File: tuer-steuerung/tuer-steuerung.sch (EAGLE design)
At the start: 14 parts, among them IC1 L6203, IC2 MEGA8-P, Q1 20MHz

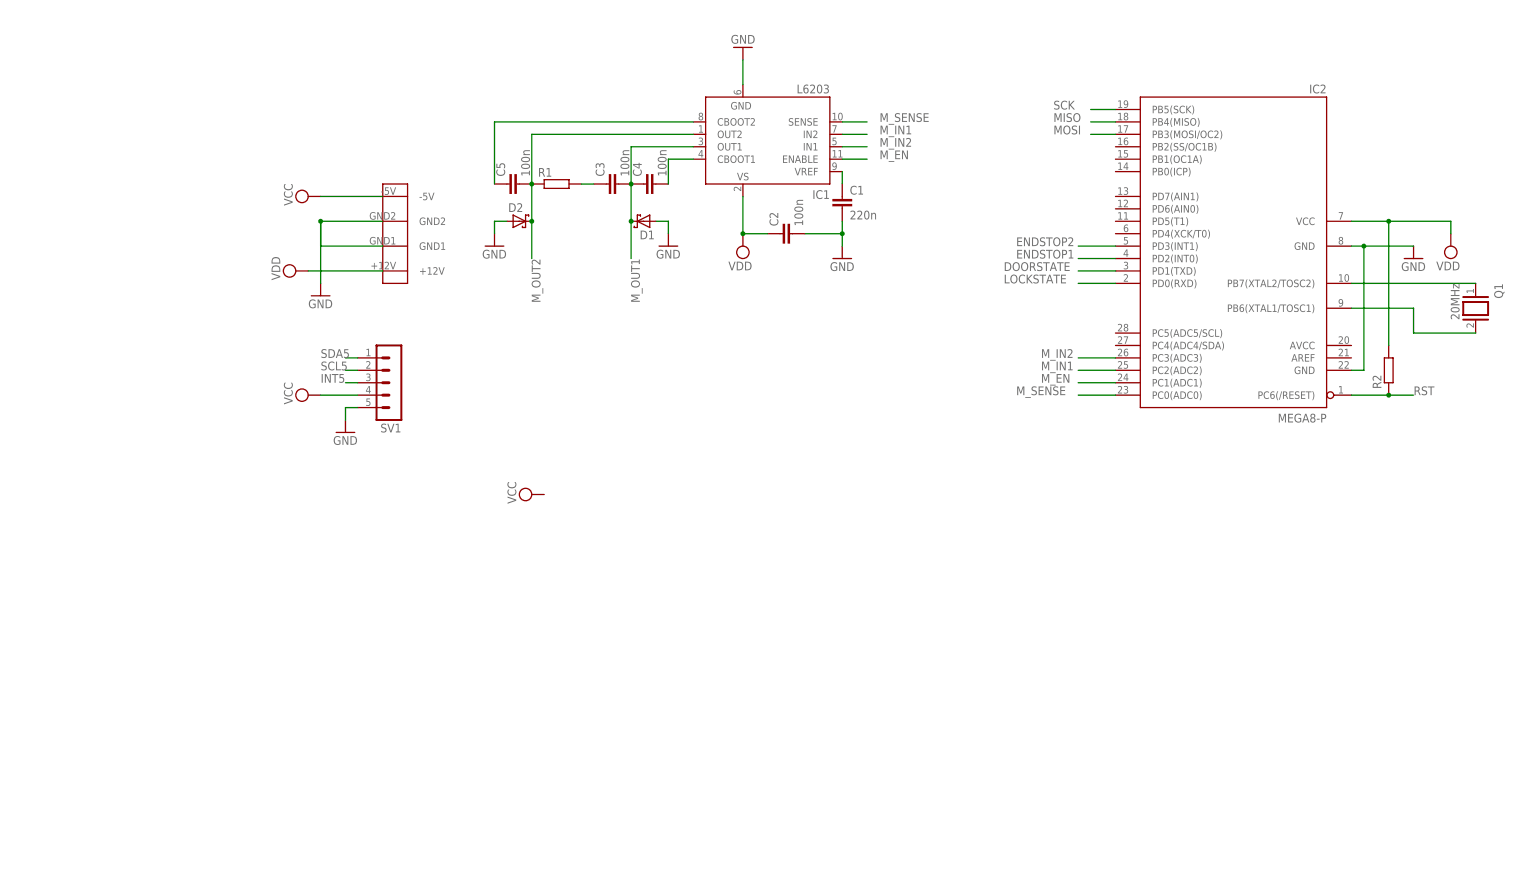
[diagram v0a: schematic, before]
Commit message: Fertige Schematics der Türsteuerung
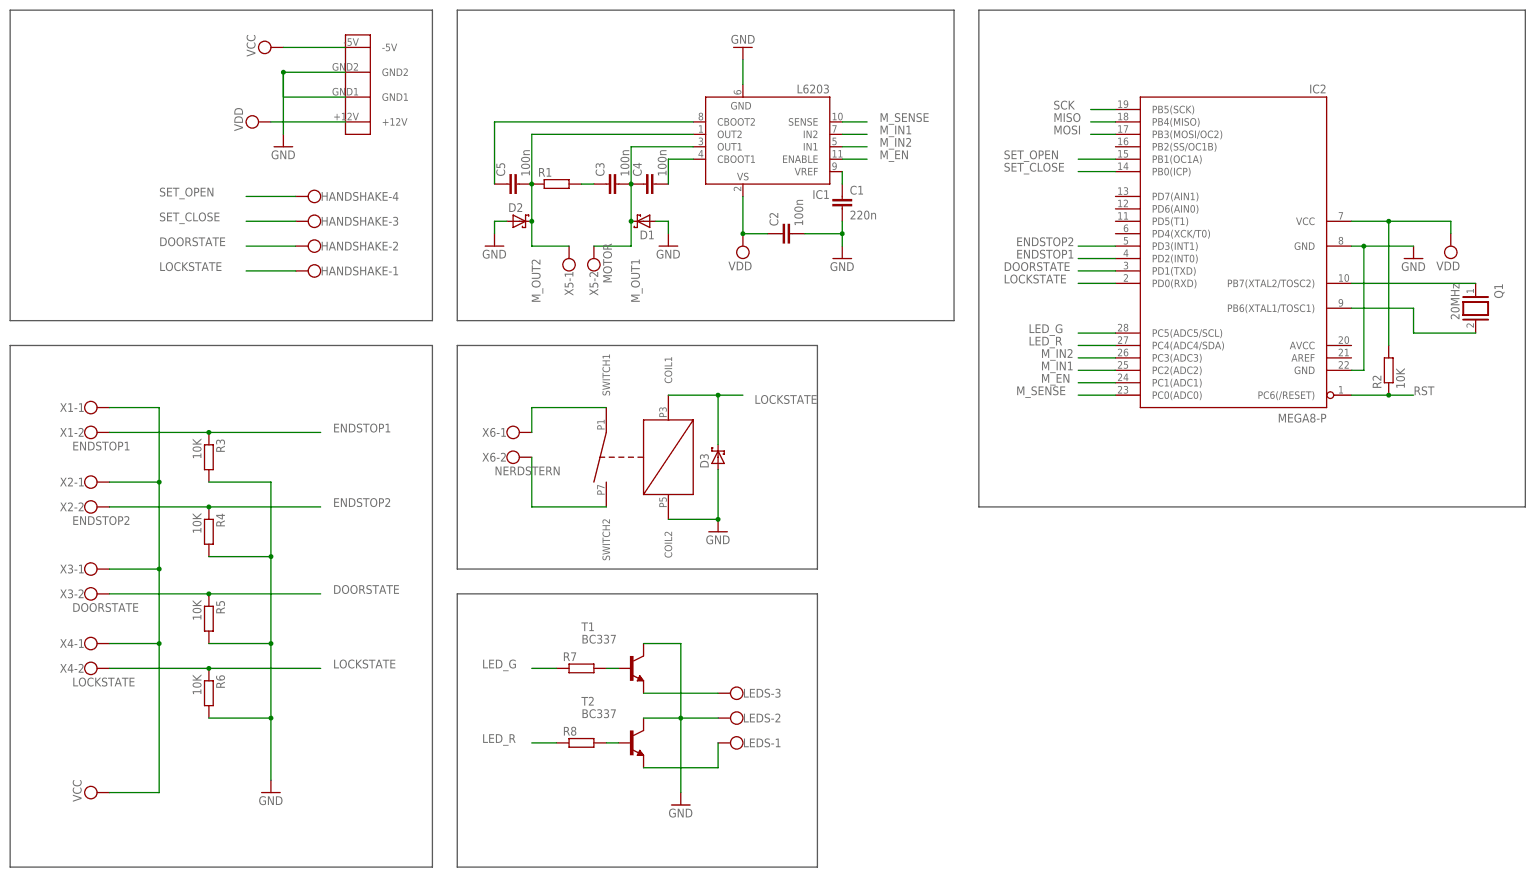
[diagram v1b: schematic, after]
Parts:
- removed SV1: (no value), con-lstb:MA05-1
- added D3: (no value), diode:SCHOTTKY-DIODEDO35-7
- added HANDSHAKE: (no value), con-wago-500:W237-4
- added LEDS: (no value), con-wago-500:W237-103
- added R3, R4, R5, R6: 10K, resistor:R-EU_0207/10
- added R7, R8: (no value), resistor:R-EU_0207/10
- added T1, T2: BC337, transistor:BC337
- added U$2: SIL05-1A72, n39:SIL05-1A72
- added X1: ENDSTOP1, con-wago-500:W237-102
- added X2: ENDSTOP2, con-wago-500:W237-102
- added X3: DOORSTATE, con-wago-500:W237-102
- added X4: LOCKSTATE, con-wago-500:W237-102
- added X5: MOTOR, con-wago-500:W237-102
- added X6: NERDSTERN, con-wago-500:W237-102
- R2: value (none) -> 10K
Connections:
- removed net INT5: SV1.3
- removed net SCL5: SV1.2
- removed net SDA5: SV1.1
- new net LED_G: IC2.PC5(ADC5/SCL), R7.1
- new net LED_R: IC2.PC4(ADC4/SDA), R8.1
- new net N$10: R8.2, T2.B
- new net N$11: LEDS-3.KL, T1.E
- new net N$12: LEDS-1.KL, T2.E
- new net N$4: X6-1.KL
- new net N$5: X6-2.KL
- new net N$9: R7.2, T1.B
- new net SET_CLOSE: HANDSHAKE-3.KL, IC2.PB0(ICP)
- new net SET_OPEN: HANDSHAKE-4.KL, IC2.PB1(OC1A)
- net DOORSTATE: now also HANDSHAKE-2.KL, R5.1, X3-2.KL
- net ENDSTOP1: now also R3.1, X1-2.KL
- net ENDSTOP2: now also R4.1, X2-2.KL
- net GND: now also D3.A, LEDS-2.KL, R3.2, R4.2, R5.2, R6.2, T1.C, T2.C; no longer SV1.5
- net LOCKSTATE: now also D3.C, HANDSHAKE-1.KL, R6.1, X4-2.KL
- net M_OUT1: now also X5-2.KL
- net M_OUT2: now also X5-1.KL
- net VCC: now also X1-1.KL, X2-1.KL, X3-1.KL, X4-1.KL; no longer SV1.4

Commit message: Schaltung Türsteuerung ergänzt
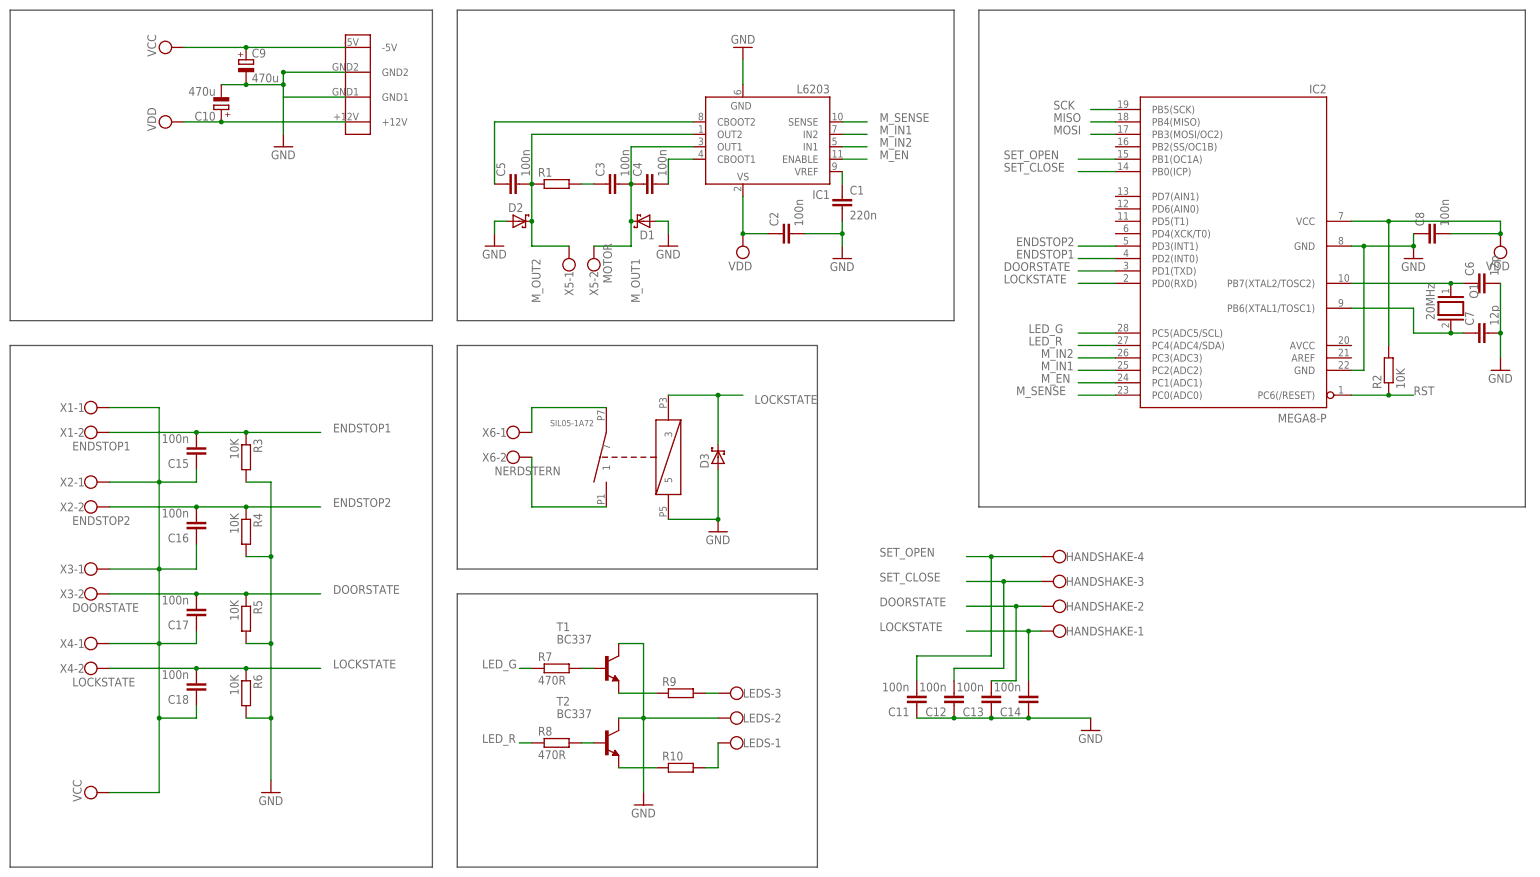
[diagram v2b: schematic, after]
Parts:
- added C10, C9: 470u, resistor:CPOL-EUTAP5-80
- added C11, C12, C13, C14, C15, C16, C17, C18: 100n, resistor:C-EUC0805K
- added C6, C7: 12p, resistor:C-EUC0805K
- added C8: 100n, resistor:C-EU025-024X044
- added R10, R9: (no value), resistor:R-EU_0207/10
- Q1: device special:XTAL -> special:XTAL/S
- R2, R3, R4, R5, R6: device resistor:R-EU_0207/10 -> resistor:R-EU_R0805W
- R7, R8: value (none) -> 470R; device resistor:R-EU_0207/10 -> resistor:R-EU_R0805W
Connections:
- new net N$13: R10.1, T2.E
- new net N$14: LEDS-1.KL, R10.2
- net DOORSTATE: now also C13.2, C17.2
- net ENDSTOP1: now also C15.2
- net ENDSTOP2: now also C16.2
- net GND: now also C10.-, C11.1, C12.1, C13.1, C14.1, C6.2, C7.2, C8.1, C9.-, U$2.5
- net LOCKSTATE: now also C14.2, C18.2, U$2.3
- net N$1: now also C6.1
- net N$11: now also R9.1; no longer LEDS-3.KL
- net N$12: now also LEDS-3.KL, R9.2; no longer LEDS-1.KL, T2.E
- net N$2: now also C7.1
- net N$4: now also U$2.7
- net N$5: now also U$2.1
- net SET_CLOSE: now also C12.2
- net SET_OPEN: now also C11.2
- net VCC: now also C15.1, C16.1, C17.1, C18.1, C9.+
- net VDD: now also C10.+, C8.2
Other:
- moved on the sheet: HANDSHAKE-1, HANDSHAKE-2, HANDSHAKE-3, HANDSHAKE-4, Q1, R3, R4, R5, R6, R7, R8, T1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

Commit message: * Kleine Anpassungen in der Schaltung * Layout der Peripherie
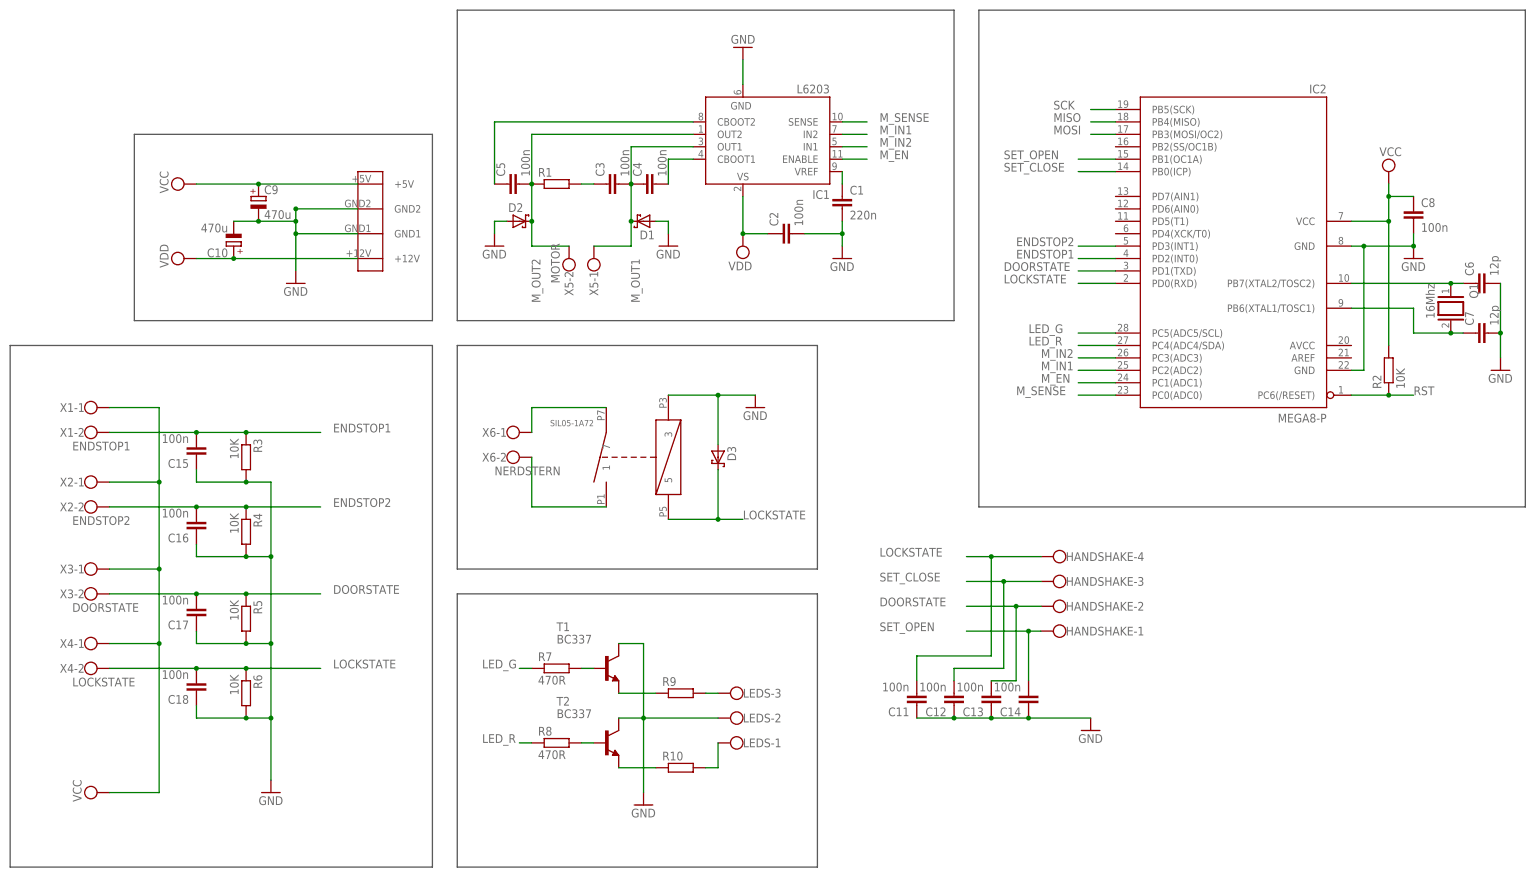
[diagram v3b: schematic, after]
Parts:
- C11, C12, C13, C14, C15, C16, C17, C18: device resistor:C-EUC0805K -> resistor:C-EU025-024X044
- C5: device resistor:C-EU025-024X044 -> resistor:C-EU050-024X044
- Q1: value 20MHz -> 16Mhz
- R1: device resistor:R-EU_0207/10 -> resistor:R-EU_0207/5V
- R10, R9: device resistor:R-EU_0207/10 -> resistor:R-EU_0207/2V
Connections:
- net GND: now also C15.1, C16.1, C17.1, C18.1, C8.2, U$2.3; no longer C8.1, U$2.5
- net LOCKSTATE: now also C11.2, HANDSHAKE-4.KL, U$2.5; no longer C14.2, HANDSHAKE-1.KL, U$2.3
- net M_OUT1: now also X5-1.KL; no longer X5-2.KL
- net M_OUT2: now also X5-2.KL; no longer X5-1.KL
- net SET_OPEN: now also C14.2, HANDSHAKE-1.KL; no longer C11.2, HANDSHAKE-4.KL
- net VCC: now also C8.1, IC2.VCC@1, R2.2, U$1.+5V; no longer C15.1, C16.1, C17.1, C18.1, U$1.-5V
- net VDD: no longer C8.2, IC2.VCC@1, R2.2
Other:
- moved on the sheet: C10, C8, C9, D3, X5-1, X5-2

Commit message: Alex' Verbesserungen eingearbeitet und Layout fortgesetzt
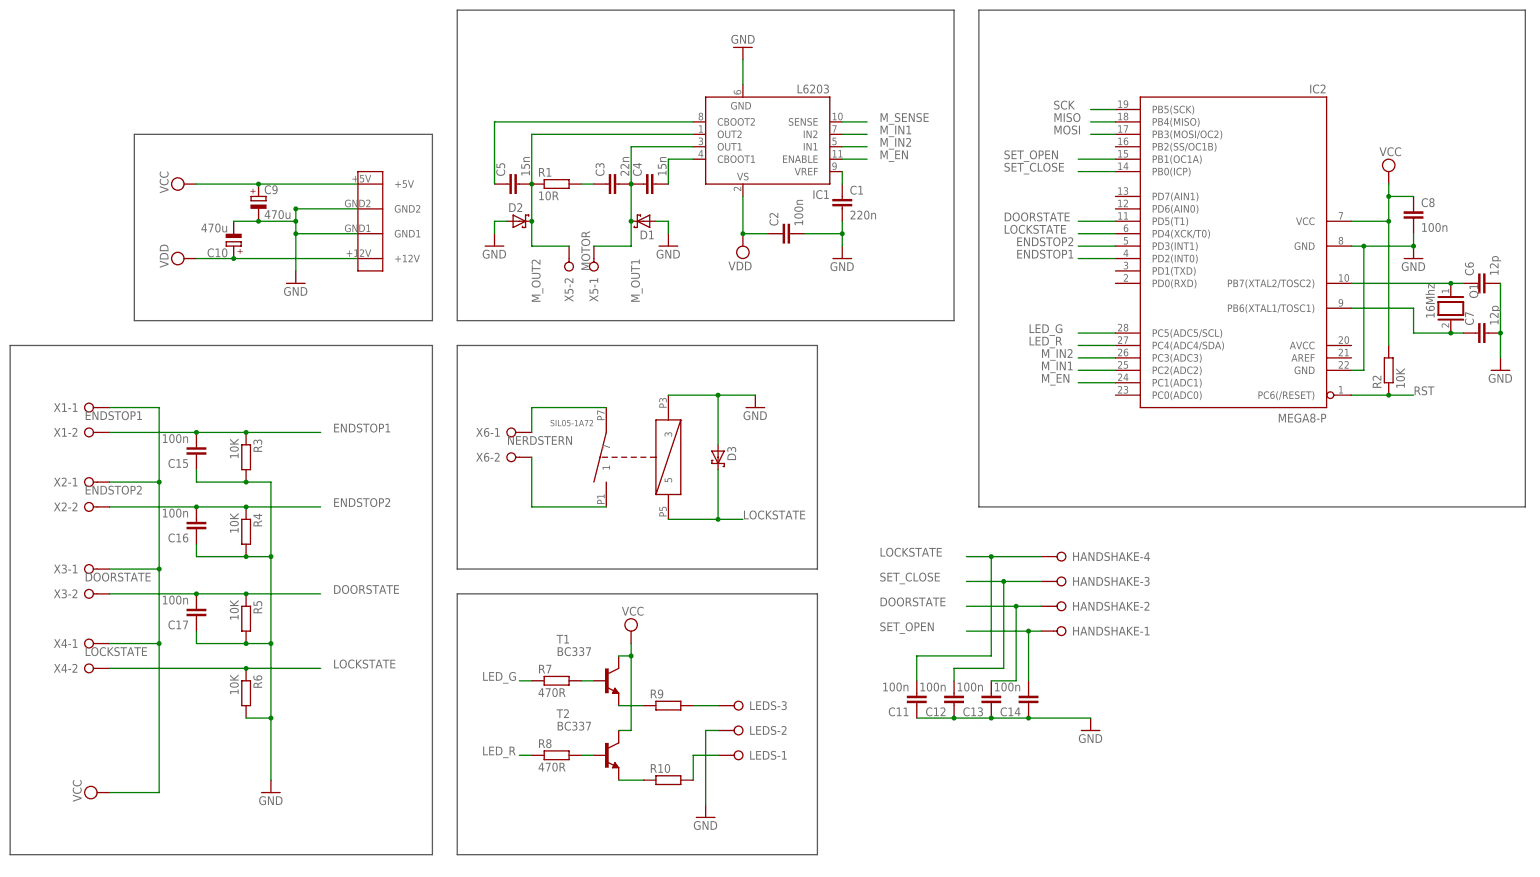
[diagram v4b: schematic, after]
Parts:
- removed C18: 100n, resistor:C-EU025-024X044
- C3: value 100n -> 22n
- C4, C5: value 100n -> 15n
- HANDSHAKE: device con-wago-500:W237-4 -> con-wago-508:W237-04P
- LEDS: device con-wago-500:W237-103 -> con-wago-508:W237-03P
- R1: value (none) -> 10R
- X1, X2, X3, X4, X5, X6: device con-wago-500:W237-102 -> con-wago-508:W237-02P
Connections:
- net DOORSTATE: now also IC2.PD5(T1); no longer IC2.PD1(TXD)
- net GND: no longer C18.1, T1.C, T2.C
- net LOCKSTATE: now also IC2.PD4(XCK/T0); no longer C18.2, IC2.PD0(RXD)
- net M_SENSE: no longer IC2.PC0(ADC0)
- net VCC: now also T1.C, T2.C
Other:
- moved on the sheet: R10, R7, R8, R9, T1, T2

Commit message: Layout vollständig (nur 3 Drahtbrücken! \o/)
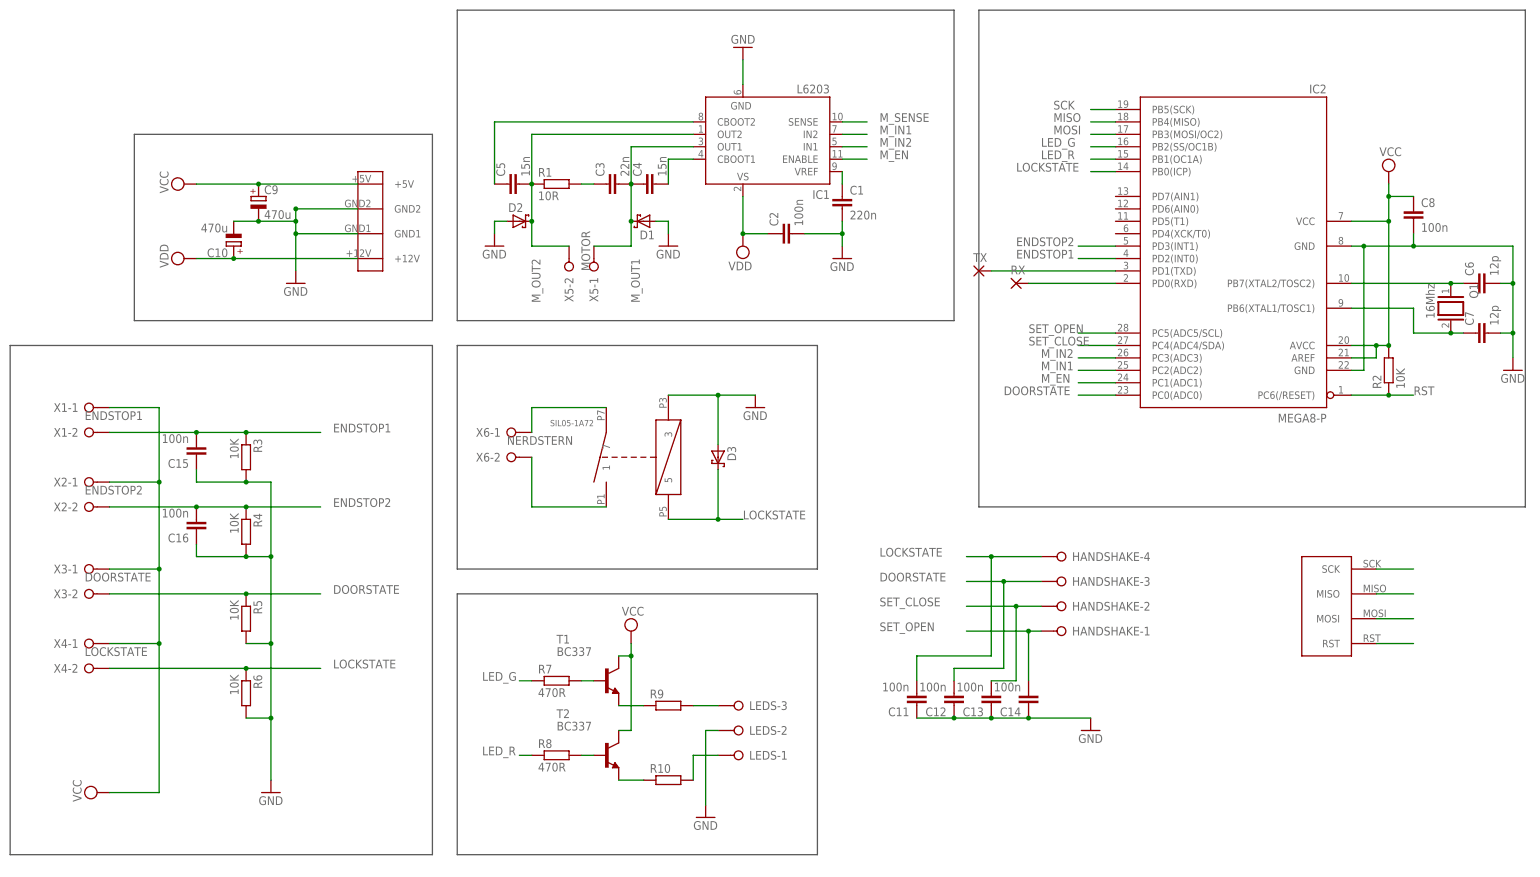
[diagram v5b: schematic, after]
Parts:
- removed C17: 100n, resistor:C-EU025-024X044
- added RX, TX: (no value), wirepad:1,6/0,9
- added U$3: AVR_ISP, n39:AVR_ISP
- R2, R7, R8: device resistor:R-EU_R0805W -> resistor:R-EU_0204/5
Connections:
- new net N$15: IC2.PD1(TXD), TX.P
- new net N$16: IC2.PD0(RXD), RX.P
- net DOORSTATE: now also C12.2, HANDSHAKE-3.KL, IC2.PC0(ADC0); no longer C13.2, C17.2, HANDSHAKE-2.KL, IC2.PD5(T1)
- net GND: no longer C17.1
- net LED_G: now also IC2.PB2(SS/OC1B); no longer IC2.PC5(ADC5/SCL)
- net LED_R: now also IC2.PB1(OC1A); no longer IC2.PC4(ADC4/SDA)
- net LOCKSTATE: now also IC2.PB0(ICP); no longer IC2.PD4(XCK/T0)
- net MISO: now also U$3.MISO
- net MOSI: now also U$3.MOSI
- net RST: now also U$3.RST
- net SCK: now also U$3.SCK
- net SET_CLOSE: now also C13.2, HANDSHAKE-2.KL, IC2.PC4(ADC4/SDA); no longer C12.2, HANDSHAKE-3.KL, IC2.PB0(ICP)
- net SET_OPEN: now also IC2.PC5(ADC5/SCL); no longer IC2.PB1(OC1A)
- net VCC: now also IC2.AREF, IC2.AVCC
